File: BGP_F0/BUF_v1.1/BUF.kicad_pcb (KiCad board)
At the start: 2 copper layers, 32 x 26 mm, 35 parts, among them P1 CONN_01X02, P2 CONN_01X02, P3 CONN_01X03, P4 CONN_01X02, P5 Conn_01x06, P6 CONN_01X05, Q1 2N5457, Q2 2N5457, U1 MC33178

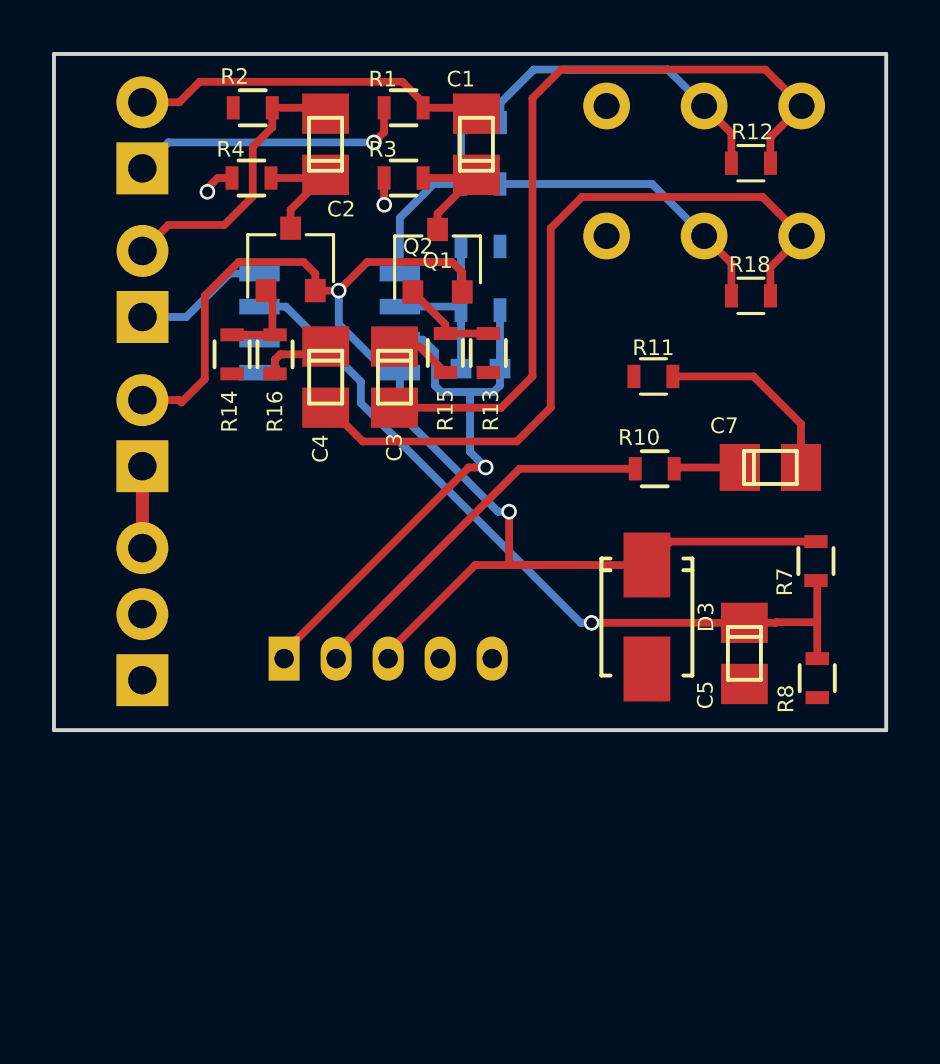
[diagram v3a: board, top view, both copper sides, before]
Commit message: Tone Pot connector and output routing added
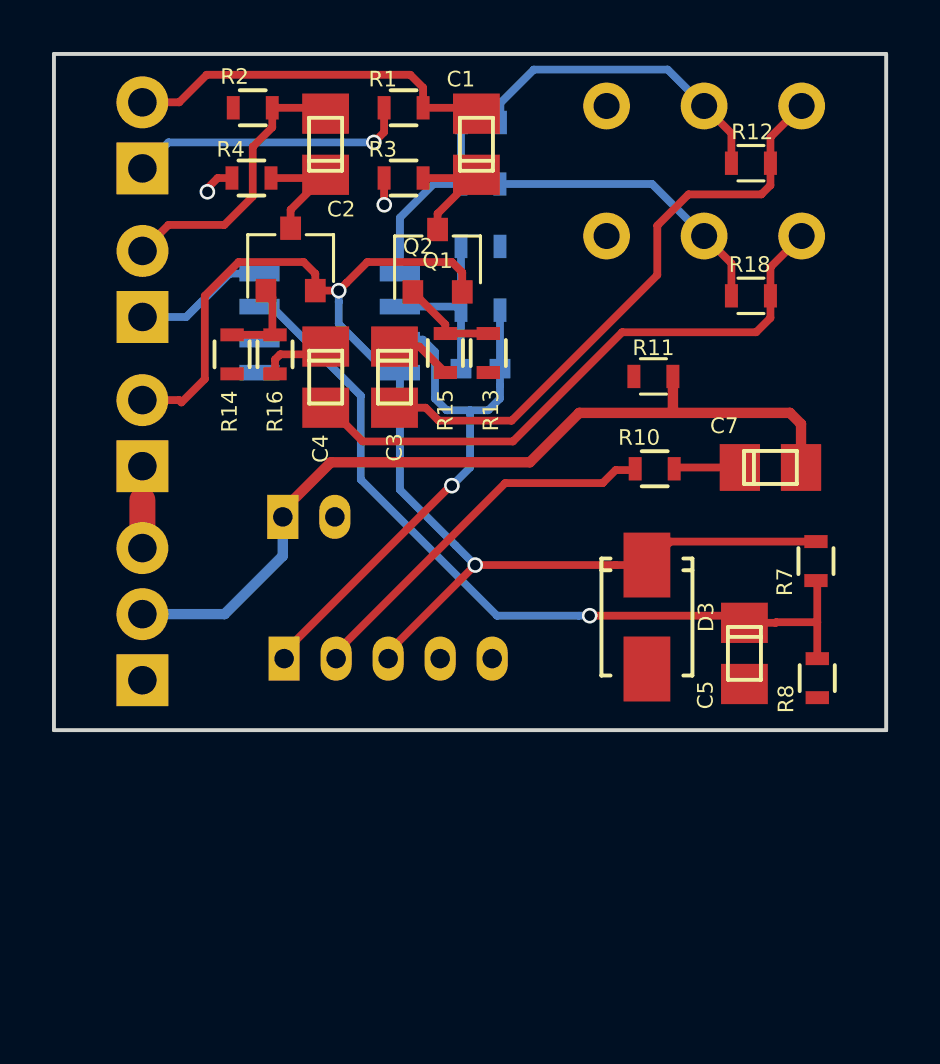
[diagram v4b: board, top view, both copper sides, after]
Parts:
- added P7: CONN_01X02, Connectors_JST:JST_PH_B2B-PH-K_02x2.00mm_Straight, B.Cu at (133.8, 95.8)
- P6: value CONN_01X05 -> Conn_01x05
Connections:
- C7 pad 2: Net-(C7-Pad2) -> /OUT
- P3 pad 2: /PV_2 -> /OUT
- R11 pad 1: Net-(C7-Pad2) -> /OUT
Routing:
- net /OUT: track 0.00 -> 33.5 mm
- net Net-(C7-Pad2): track 8.26 -> 0.00 mm
- net /PB1_1: track 30.7 -> 23.1 mm
- net /PB2_1: track 30.2 -> 23.3 mm
- net /V+: track 54.0 -> 50.1 mm
- net Net-(C5-Pad1): track 30.1 -> 31.5 mm
- net /IN_N: track 13.8 -> 14.4 mm

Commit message: F0 Vol/Vol spec LOG pots
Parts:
- removed R12, R18: 12k, Resistors_SMD:R_0603
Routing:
- net /PB2_2: track 11.4 -> 8.68 mm
- net /PB1_2: track 12.3 -> 9.70 mm
- net /PB2_1: track 23.3 -> 22.1 mm
- net /PB1_1: track 23.1 -> 22.2 mm
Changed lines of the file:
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@@
 (kicad_pcb (version 4) (host pcbnew 4.0.7)
   (general
-    (links 65)
+    (links 61)
     (no_connects 0)
     (area 124.924999 77.924999 157.075001 104.075001)
     (thickness 1.2)
     (drawings 8)
-    (tracks 180)
+    (tracks 170)
     (zones 0)
-    (modules 36)
+    (modules 34)
     (nets 24)
   )
@@
     )
   )
-  (module Resistors_SMD:R_0603 (layer F.Cu)
-    (at 151.8 82.2)
-    (descr "Resistor SMD 0603, reflow soldering, Vishay (see dcrcw.pdf)")
-    (tags "resistor 0603")
-    (attr smd)
-    (fp_text reference R12 (at 0.05 -1.2) (layer F.SilkS)
-      (effects (font (size 0.6 0.6) (thickness 0.15)))
-    )
-    (fp_text value 12k (at 0 1.5) (layer F.Fab) hide
-      (effects (font (size 0.6 0.6) (thickness 0.15)))
-    )
-    (fp_text user %R (at 0 0) (layer F.Fab) hide
-      (effects (font (size 0.4 0.4) (thickness 0.075)))
-    )
-    (fp_line (start -0.8 0.4) (end -0.8 -0.4) (layer F.Fab) (width 0.1))
-    (fp_line (start 0.8 0.4) (end -0.8 0.4) (layer F.Fab) (width 0.1))
-    (fp_line (start 0.8 -0.4) (end 0.8 0.4) (layer F.Fab) (width 0.1))
-    (fp_line (start -0.8 -0.4) (end 0.8 -0.4) (layer F.Fab) (width 0.1))
-    (fp_line (start 0.5 0.68) (end -0.5 0.68) (layer F.SilkS) (width 0.12))
-    (fp_line (start -0.5 -0.68) (end 0.5 -0.68) (layer F.SilkS) (width 0.12))
-    (fp_line (start -1.25 -0.7) (end 1.25 -0.7) (layer F.CrtYd) (width 0.05))
-    (fp_line (start -1.25 -0.7) (end -1.25 0.7) (layer F.CrtYd) (width 0.05))
-    (fp_line (start 1.25 0.7) (end 1.25 -0.7) (layer F.CrtYd) (width 0.05))
-    (fp_line (start 1.25 0.7) (end -1.25 0.7) (layer F.CrtYd) (width 0.05))
-    (pad 1 smd rect (at -0.75 0) (size 0.5 0.9) (layers F.Cu F.Paste F.Mask)
-      (net 14 /PB1_2))
-    (pad 2 smd rect (at 0.75 0) (size 0.5 0.9) (layers F.Cu F.Paste F.Mask)
-      (net 4 /PB1_1))
-    (model ${KISYS3DMOD}/Resistors_SMD.3dshapes/R_0603.wrl
-      (at (xyz 0 0 0))
-      (scale (xyz 1 1 1))
-      (rotate (xyz 0 0 0))
-    )
-  )
-  (module Resistors_SMD:R_0603 (layer F.Cu)
-    (at 151.8 87.3)
-    (descr "Resistor SMD 0603, reflow soldering, Vishay (see dcrcw.pdf)")
-    (tags "resistor 0603")
-    (attr smd)
-    (fp_text reference R18 (at -0.05 -1.2) (layer F.SilkS)
-      (effects (font (size 0.6 0.6) (thickness 0.15)))
-    )
-    (fp_text value 12k (at 0 1.5) (layer F.Fab) hide
-      (effects (font (size 0.6 0.6) (thickness 0.15)))
-    )
-    (fp_text user %R (at 0 0) (layer F.Fab) hide
-      (effects (font (size 0.4 0.4) (thickness 0.075)))
-    )
-    (fp_line (start -0.8 0.4) (end -0.8 -0.4) (layer F.Fab) (width 0.1))
-    (fp_line (start 0.8 0.4) (end -0.8 0.4) (layer F.Fab) (width 0.1))
-    (fp_line (start 0.8 -0.4) (end 0.8 0.4) (layer F.Fab) (width 0.1))
-    (fp_line (start -0.8 -0.4) (end 0.8 -0.4) (layer F.Fab) (width 0.1))
-    (fp_line (start 0.5 0.68) (end -0.5 0.68) (layer F.SilkS) (width 0.12))
-    (fp_line (start -0.5 -0.68) (end 0.5 -0.68) (layer F.SilkS) (width 0.12))
-    (fp_line (start -1.25 -0.7) (end 1.25 -0.7) (layer F.CrtYd) (width 0.05))
-    (fp_line (start -1.25 -0.7) (end -1.25 0.7) (layer F.CrtYd) (width 0.05))
-    (fp_line (start 1.25 0.7) (end 1.25 -0.7) (layer F.CrtYd) (width 0.05))
-    (fp_line (start 1.25 0.7) (end -1.25 0.7) (layer F.CrtYd) (width 0.05))
-    (pad 1 smd rect (at -0.75 0) (size 0.5 0.9) (layers F.Cu F.Paste F.Mask)
-      (net 15 /PB2_2))
-    (pad 2 smd rect (at 0.75 0) (size 0.5 0.9) (layers F.Cu F.Paste F.Mask)
-      (net 22 /PB2_1))
-    (model ${KISYS3DMOD}/Resistors_SMD.3dshapes/R_0603.wrl
-      (at (xyz 0 0 0))
-      (scale (xyz 1 1 1))
-      (rotate (xyz 0 0 0))
-    )
-  )
   (module Connectors_JST:JST_PH_B2B-PH-K_02x2.00mm_Straight (layer B.Cu)
     (at 133.8 95.8)
@@
   (segment (start 139.05 89.25) (end 140.05 90.25) (width 0.3) (layer F.Cu) (net 3))
   (segment (start 138.093993 91.60204) (end 139.294423 91.60204) (width 0.3) (layer F.Cu) (net 4))
-  (segment (start 149.4 83.4) (end 152.2 83.4) (width 0.3) (layer F.Cu) (net 4))
   (segment (start 139.294423 91.60204) (end 139.792383 92.1) (width 0.3) (layer F.Cu) (net 4))
   (segment (start 139.792383 92.1) (end 142.6 92.1) (width 0.3) (layer F.Cu) (net 4))
+  (segment (start 148.2 84.3) (end 152.4 80.1) (width 0.3) (layer F.Cu) (net 4))
   (segment (start 142.6 92.1) (end 148.2 86.5) (width 0.3) (layer F.Cu) (net 4))
-  (segment (start 148.2 86.5) (end 148.2 84.6) (width 0.3) (layer F.Cu) (net 4))
-  (segment (start 152.55 83.05) (end 152.55 82.2) (width 0.3) (layer F.Cu) (net 4))
-  (segment (start 148.2 84.6) (end 149.4 83.4) (width 0.3) (layer F.Cu) (net 4))
-  (segment (start 152.2 83.4) (end 152.55 83.05) (width 0.3) (layer F.Cu) (net 4))
-  (segment (start 152.55 82.2) (end 152.55 81.2) (width 0.3) (layer F.Cu) (net 4))
-  (segment (start 152.55 81.2) (end 153.75 80) (width 0.3) (layer F.Cu) (net 4))
+  (segment (start 148.2 86.5) (end 148.2 84.3) (width 0.3) (layer F.Cu) (net 4))
+  (segment (start 152.4 80.1) (end 153.65 80.1) (width 0.3) (layer F.Cu) (net 4))
+  (segment (start 153.65 80.1) (end 153.75 80) (width 0.3) (layer F.Cu) (net 4))
   (segment (start 133.7 89.55) (end 135.12398 89.55) (width 0.3) (layer F.Cu) (net 5))
   (segment (start 135.12398 89.55) (end 135.45 89.22398) (width 0.3) (layer F.Cu) (net 5))
@@
   (segment (start 131.843993 82.770255) (end 131.293993 82.770255) (width 0.3) (layer F.Cu) (net 13))
   (via (at 130.9 83.3) (size 0.6) (drill 0.4) (layers F.Cu B.Cu) (net 13))
-  (segment (start 146.2 85) (end 146.25 85) (width 0.3) (layer F.Cu) (net 13))
-  (segment (start 151.05 82.2) (end 151.05 81.05) (width 0.3) (layer F.Cu) (net 14))
-  (segment (start 151.05 81.05) (end 150 80) (width 0.3) (layer F.Cu) (net 14))
   (segment (start 143.45 78.6) (end 148.6 78.6) (width 0.3) (layer B.Cu) (net 14))
   (segment (start 148.6 78.6) (end 150 80) (width 0.3) (layer B.Cu) (net 14))
   (segment (start 142.164739 80.635261) (end 142.164739 79.885261) (width 0.3) (layer B.Cu) (net 14))
   (segment (start 142.164739 79.885261) (end 143.45 78.6) (width 0.3) (layer B.Cu) (net 14))
-  (segment (start 151.05 87.3) (end 151.05 86.05) (width 0.3) (layer F.Cu) (net 15))
-  (segment (start 151.05 86.05) (end 150 85) (width 0.3) (layer F.Cu) (net 15))
   (segment (start 150 85) (end 148 83) (width 0.3) (layer B.Cu) (net 15))
   (segment (start 148 83) (end 142.15 83) (width 0.3) (layer B.Cu) (net 15))
@@
   (segment (start 128.4 95.14949) (end 128.4 97) (width 1) (layer F.Cu) (net 21))
   (segment (start 135.45 91.60204) (end 135.57573 91.60204) (width 0.3) (layer F.Cu) (net 22))
+  (segment (start 152.4 85) (end 153.75 85) (width 0.3) (layer F.Cu) (net 22))
   (segment (start 135.57573 91.60204) (end 136.873678 92.899988) (width 0.3) (layer F.Cu) (net 22))
-  (segment (start 146.848542 88.7) (end 152 88.7) (width 0.3) (layer F.Cu) (net 22))
   (segment (start 136.873678 92.899988) (end 142.648554 92.899988) (width 0.3) (layer F.Cu) (net 22))
-  (segment (start 142.648554 92.899988) (end 146.848542 88.7) (width 0.3) (layer F.Cu) (net 22))
-  (segment (start 152.55 88.15) (end 152.55 87.3) (width 0.3) (layer F.Cu) (net 22))
-  (segment (start 152 88.7) (end 152.55 88.15) (width 0.3) (layer F.Cu) (net 22))
-  (segment (start 152.55 87.3) (end 152.55 86.2) (width 0.3) (layer F.Cu) (net 22))
-  (segment (start 152.55 86.2) (end 153.75 85) (width 0.3) (layer F.Cu) (net 22))
+  (segment (start 142.648554 92.899988) (end 148.348542 87.2) (width 0.3) (layer F.Cu) (net 22))
+  (segment (start 148.348542 87.2) (end 150.2 87.2) (width 0.3) (layer F.Cu) (net 22))
+  (segment (start 150.2 87.2) (end 152.4 85) (width 0.3) (layer F.Cu) (net 22))
   (segment (start 128.4 99.54) (end 131.56 99.54) (width 0.4) (layer B.Cu) (net 23))
   (segment (start 131.56 99.54) (end 133.8 97.3) (width 0.4) (layer B.Cu) (net 23))

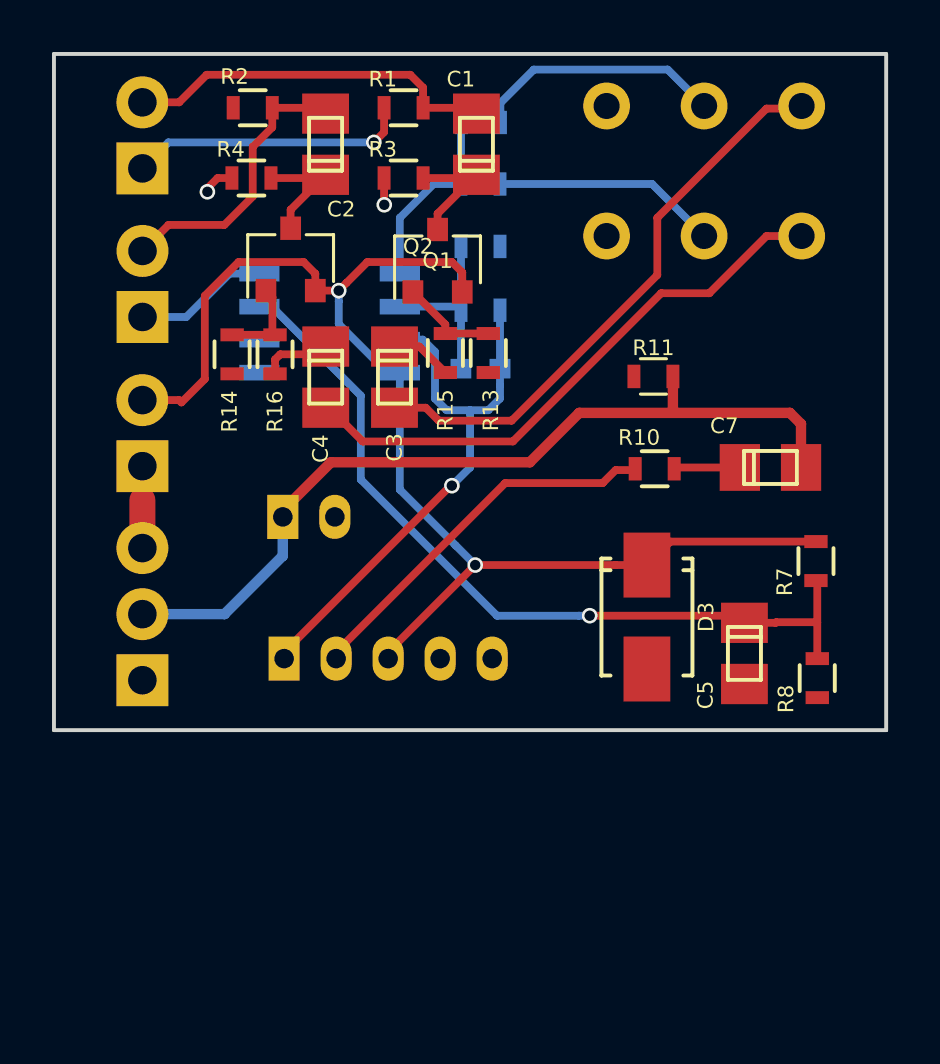
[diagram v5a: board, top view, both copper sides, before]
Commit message: F0 - BUF JFET bypass caps at i/p
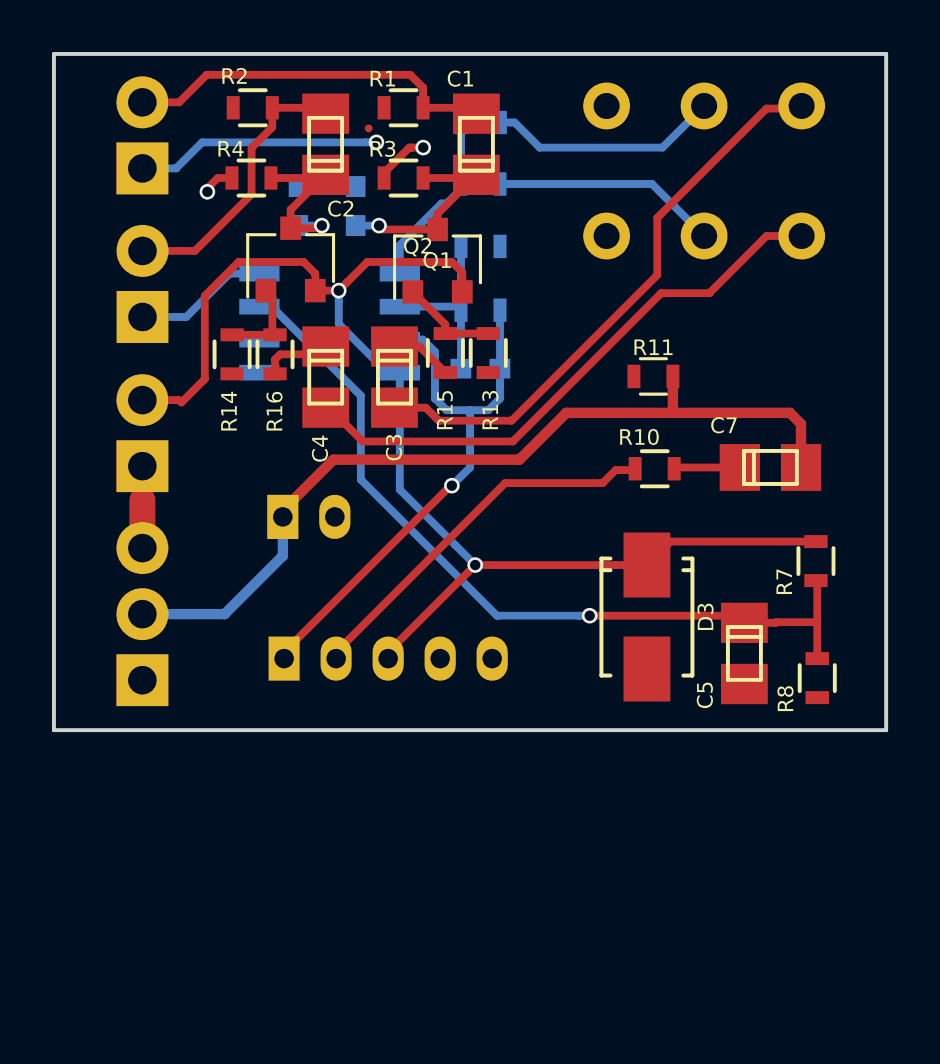
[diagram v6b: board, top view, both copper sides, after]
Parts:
- added C8: 270p, Capacitors_SMD:C_0603, B.Cu at (136.6, 83.8)
- added C9: 270p, Capacitors_SMD:C_0603, B.Cu at (134.4, 83.8)
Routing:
- net Net-(C1-Pad1): track 4.82 -> 8.24 mm, vias 0 -> 1
- net Net-(C2-Pad1): track 4.76 -> 6.90 mm, vias 0 -> 1
- net Earth: track 16.0 -> 14.8 mm
- net /VRef: track 2.28 -> 3.40 mm
- net /PB1_2: track 9.70 -> 8.90 mm

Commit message: Various
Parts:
- R5, R6: value 4.7k -> 100k
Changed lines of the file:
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@@
-(kicad_pcb (version 4) (host pcbnew 4.0.7)
+(kicad_pcb (version 4) (host pcbnew 4.0.4-1.fc24-product)
   (general
     (links 65)
@@
       (effects (font (size 0.6 0.6) (thickness 0.15)) (justify mirror))
     )
-    (fp_text value 4.7k (at 0 -1.9) (layer B.Fab) hide
+    (fp_text value 100k (at 0 -1.9) (layer B.Fab) hide
       (effects (font (size 0.6 0.6) (thickness 0.15)) (justify mirror))
     )
@@
       (effects (font (size 0.6 0.6) (thickness 0.15)) (justify mirror))
     )
-    (fp_text value 4.7k (at 0 -1.9) (layer B.Fab) hide
+    (fp_text value 100k (at 0 -1.9) (layer B.Fab) hide
       (effects (font (size 0.6 0.6) (thickness 0.15)) (justify mirror))
     )
@@
   (gr_line (start 125 78) (end 125 104) (layer Edge.Cuts) (width 0.15))
   (gr_line (start 157 78) (end 125 78) (layer Edge.Cuts) (width 0.15))
+  (segment (start 137.103316 80.860932) (end 137.100001 80.864247) (width 0.3) (layer F.Cu) (net 0))
   (segment (start 137.650008 84.75) (end 137.500008 84.6) (width 0.3) (layer F.Cu) (net 1))
   (segment (start 139.75 84.75) (end 137.650008 84.75) (width 0.3) (layer F.Cu) (net 1))
@@
   (segment (start 128.4 82.4) (end 129.69949 82.4) (width 0.3) (layer B.Cu) (net 7))
   (via (at 137.4 81.400016) (size 0.6) (drill 0.4) (layers F.Cu B.Cu) (net 7))
-  (segment (start 137.103316 80.860932) (end 137.100001 80.864247) (width 0.3) (layer F.Cu) (net 7))
   (segment (start 137.693993 80.070255) (end 137.693993 80.270255) (width 0.3) (layer F.Cu) (net 7))
   (segment (start 132.9 86.445) (end 131.755 86.445) (width 0.3) (layer B.Cu) (net 7))
